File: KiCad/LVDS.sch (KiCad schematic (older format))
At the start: 7 parts, among them J1 RJ45_Shielded, U1 DS90LV049TMT

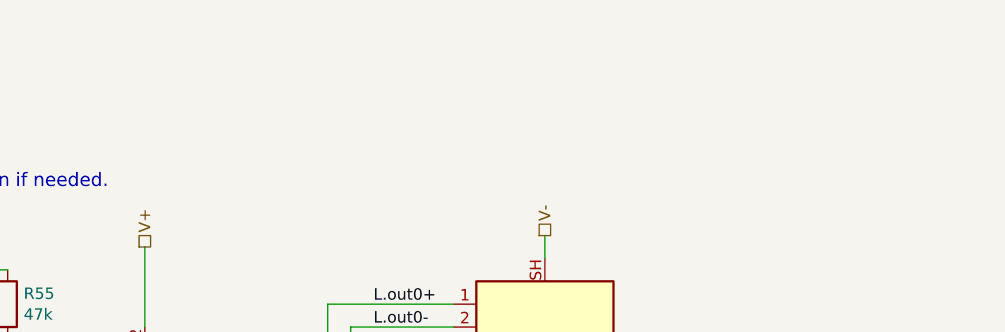
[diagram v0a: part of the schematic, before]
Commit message: Added impedance calc, and rerouted USB
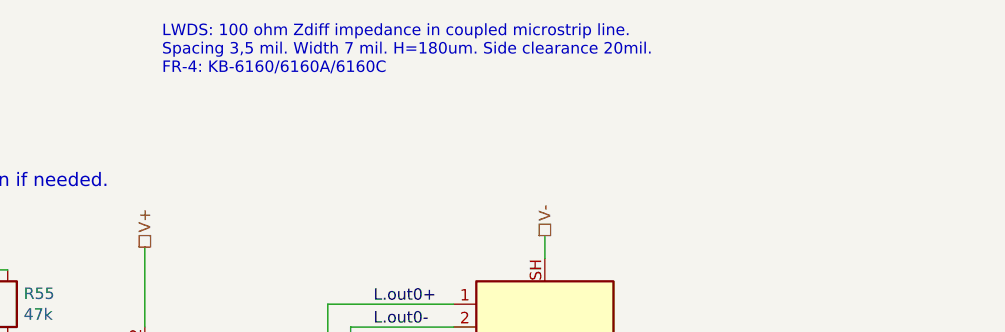
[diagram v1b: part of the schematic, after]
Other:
- note added: "LWDS: 100 ohm Zdiff impedance in coupled microstrip line.\nSpacing 3,5 mil. Width 7 mil. H=180um. Side clearance 20mil.\nFR-4: KB-6160/6160A/6160C"
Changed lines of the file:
@@
 Text Label 3500 3825 0    50   ~ 0
 L.in1-
+Text Notes 2900 1675 0    50   ~ 0
+LWDS: 100 ohm Zdiff impedance in coupled microstrip line.\nSpacing 3,5 mil. Width 7 mil. H=180um. Side clearance 20mil.\nFR-4: KB-6160/6160A/6160C
 $EndSCHEMATC

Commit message: Many small fixes
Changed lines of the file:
@@
 AR Path="/5CAE894D/5C318F8C" Ref="J14"  Part="1"
 AR Path="/5CC36DF5/5C318F8C" Ref="J19"  Part="1"
-F 0 "J19" H 4246 3016 50  0000 R CNN
+F 0 "J16" H 4246 3016 50  0000 R CNN
 F 1 "RJ45_Shielded" H 4246 2925 50  0000 R CNN
 F 2 "Connector_RJ:RJ45_Amphenol_RJHSE5380" V 4575 3000 50  0001 C CNN
@@
 AR Path="/5CAE894D/5C1F0997" Ref="U15"  Part="1"
 AR Path="/5CC36DF5/5C1F0997" Ref="U20"  Part="1"
-F 0 "U20" H 2525 3325 50  0000 L CNN
+F 0 "U16" H 2525 3325 50  0000 L CNN
 F 1 "DS90LV049TMT" H 2925 2125 50  0000 L CNN
 F 2 "Package_SO:TSSOP-16_4.4x5mm_P0.65mm" H 2625 3075 50  0001 C CNN
@@
 AR Path="/5CAE894D/5C318FC1" Ref="C47"  Part="1"
 AR Path="/5CC36DF5/5C318FC1" Ref="C53"  Part="1"
-F 0 "C53" H 1840 4521 50  0000 L CNN
+F 0 "C48" H 1840 4521 50  0000 L CNN
 F 1 "100nF" H 1840 4430 50  0000 L CNN
 F 2 "Capacitor_SMD:C_0603_1608Metric_Pad1.05x0.95mm_HandSolder" H 1763 4325 50  0001 C CNN
@@
 AR Path="/5CAE894D/5E2282E6" Ref="R37"  Part="1"
 AR Path="/5CC36DF5/5E2282E6" Ref="R56"  Part="1"
-F 0 "R56" H 4145 4021 50  0000 L CNN
+F 0 "R44" H 4145 4021 50  0000 L CNN
 F 1 "100R" H 4145 3930 50  0000 L CNN
 F 2 "Resistor_SMD:R_0402_1005Metric" V 4005 3975 50  0001 C CNN
@@
 AR Path="/5CAE894D/5E22A193" Ref="R38"  Part="1"
 AR Path="/5CC36DF5/5E22A193" Ref="R57"  Part="1"
-F 0 "R57" H 4595 3771 50  0000 L CNN
+F 0 "R45" H 4595 3771 50  0000 L CNN
 F 1 "100R" H 4595 3680 50  0000 L CNN
 F 2 "Resistor_SMD:R_0402_1005Metric" V 4455 3725 50  0001 C CNN
@@
 AR Path="/5CAE894D/5C319046" Ref="R36"  Part="1"
 AR Path="/5CC36DF5/5C319046" Ref="R55"  Part="1"
-F 0 "R55" H 2295 2721 50  0000 L CNN
+F 0 "R43" H 2295 2721 50  0000 L CNN
 F 1 "47k" H 2295 2630 50  0000 L CNN
 F 2 "Resistor_SMD:R_0402_1005Metric" V 2155 2675 50  0001 C CNN
@@
 AR Path="/5CAE894D/5E5F7C9F" Ref="R35"  Part="1"
 AR Path="/5CC36DF5/5E5F7C9F" Ref="R54"  Part="1"
-F 0 "R54" H 1945 2721 50  0000 L CNN
+F 0 "R42" H 1945 2721 50  0000 L CNN
 F 1 "47k" H 1945 2630 50  0000 L CNN
 F 2 "Resistor_SMD:R_0402_1005Metric" V 1805 2675 50  0001 C CNN
